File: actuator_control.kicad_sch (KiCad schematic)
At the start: 5 parts, among them J4 Conn_01x02, Q1 BSS138

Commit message: do some pcb routing
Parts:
- J7: renamed from J4; footprint Connector_JST:JST_EH_B2B-EH-A_1x02_P2.50mm_Vertical -> Connector_Molex:Molex_Micro-Fit_3.0_43650-0215_1x02_P3.00mm_Vertical
- renumbered D10 to D11, Q1 to Q2, R26 to R24, R27 to R25
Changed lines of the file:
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@@
 		(dnp no)
 		(fields_autoplaced yes)
-		(property "Reference" "D10"
+		(property "Reference" "D11"
 			(at 138.176 90.17 0)
 			(show_name no)
@@
 			(project "gse_control_node"
 				(path "/24817451-dfe0-4b9a-9d93-7304529c9d58/3ca34fcb-848a-442f-9018-9caf10b9e369"
+					(reference "D13")
+					(unit 1)
+				)
+				(path "/24817451-dfe0-4b9a-9d93-7304529c9d58/93ade7e9-ef13-409d-a430-89296b231c7f"
 					(reference "D12")
 					(unit 1)
 				)
-				(path "/24817451-dfe0-4b9a-9d93-7304529c9d58/93ade7e9-ef13-409d-a430-89296b231c7f"
+				(path "/24817451-dfe0-4b9a-9d93-7304529c9d58/c4e569fb-235e-4777-b718-8e9c9d97ed61"
+					(reference "D14")
+					(unit 1)
+				)
+				(path "/24817451-dfe0-4b9a-9d93-7304529c9d58/fe2b7ba1-9565-4f89-9bf9-1d97bef2da17"
 					(reference "D11")
-					(unit 1)
-				)
-				(path "/24817451-dfe0-4b9a-9d93-7304529c9d58/c4e569fb-235e-4777-b718-8e9c9d97ed61"
-					(reference "D13")
-					(unit 1)
-				)
-				(path "/24817451-dfe0-4b9a-9d93-7304529c9d58/fe2b7ba1-9565-4f89-9bf9-1d97bef2da17"
-					(reference "D10")
 					(unit 1)
 				)
@@
 		(dnp no)
 		(fields_autoplaced yes)
-		(property "Reference" "R27"
+		(property "Reference" "R25"
 			(at 133.35 106.6799 0)
 			(show_name no)
@@
 			(project "gse_control_node"
 				(path "/24817451-dfe0-4b9a-9d93-7304529c9d58/3ca34fcb-848a-442f-9018-9caf10b9e369"
+					(reference "R29")
+					(unit 1)
+				)
+				(path "/24817451-dfe0-4b9a-9d93-7304529c9d58/93ade7e9-ef13-409d-a430-89296b231c7f"
+					(reference "R27")
+					(unit 1)
+				)
+				(path "/24817451-dfe0-4b9a-9d93-7304529c9d58/c4e569fb-235e-4777-b718-8e9c9d97ed61"
 					(reference "R31")
 					(unit 1)
 				)
-				(path "/24817451-dfe0-4b9a-9d93-7304529c9d58/93ade7e9-ef13-409d-a430-89296b231c7f"
-					(reference "R29")
-					(unit 1)
-				)
-				(path "/24817451-dfe0-4b9a-9d93-7304529c9d58/c4e569fb-235e-4777-b718-8e9c9d97ed61"
-					(reference "R33")
-					(unit 1)
-				)
 				(path "/24817451-dfe0-4b9a-9d93-7304529c9d58/fe2b7ba1-9565-4f89-9bf9-1d97bef2da17"
-					(reference "R27")
+					(reference "R25")
 					(unit 1)
 				)
@@
 		(dnp no)
 		(fields_autoplaced yes)
-		(property "Reference" "#PWR0195"
+		(property "Reference" "#PWR071"
 			(at 130.81 97.79 0)
 			(hide yes)
@@
 			(project "gse_control_node"
 				(path "/24817451-dfe0-4b9a-9d93-7304529c9d58/3ca34fcb-848a-442f-9018-9caf10b9e369"
-					(reference "#PWR0203")
+					(reference "#PWR079")
 					(unit 1)
 				)
 				(path "/24817451-dfe0-4b9a-9d93-7304529c9d58/93ade7e9-ef13-409d-a430-89296b231c7f"
-					(reference "#PWR0197")
+					(reference "#PWR075")
 					(unit 1)
 				)
 				(path "/24817451-dfe0-4b9a-9d93-7304529c9d58/c4e569fb-235e-4777-b718-8e9c9d97ed61"
-					(reference "#PWR0207")
+					(reference "#PWR083")
 					(unit 1)
 				)
 				(path "/24817451-dfe0-4b9a-9d93-7304529c9d58/fe2b7ba1-9565-4f89-9bf9-1d97bef2da17"
-					(reference "#PWR0195")
+					(reference "#PWR071")
 					(unit 1)
 				)
@@
 		(in_pos_files yes)
 		(dnp no)
-		(property "Reference" "#PWR0198"
+		(property "Reference" "#PWR072"
 			(at 130.81 116.84 0)
 			(hide yes)
@@
 			(project "gse_control_node"
 				(path "/24817451-dfe0-4b9a-9d93-7304529c9d58/3ca34fcb-848a-442f-9018-9caf10b9e369"
-					(reference "#PWR0204")
+					(reference "#PWR080")
 					(unit 1)
 				)
 				(path "/24817451-dfe0-4b9a-9d93-7304529c9d58/93ade7e9-ef13-409d-a430-89296b231c7f"
-					(reference "#PWR0200")
+					(reference "#PWR076")
 					(unit 1)
 				)
 				(path "/24817451-dfe0-4b9a-9d93-7304529c9d58/c4e569fb-235e-4777-b718-8e9c9d97ed61"
-					(reference "#PWR0208")
+					(reference "#PWR084")
 					(unit 1)
 				)
 				(path "/24817451-dfe0-4b9a-9d93-7304529c9d58/fe2b7ba1-9565-4f89-9bf9-1d97bef2da17"
-					(reference "#PWR0198")
+					(reference "#PWR072")
 					(unit 1)
 				)
@@
 		(dnp no)
 		(fields_autoplaced yes)
-		(property "Reference" "#PWR0196"
+		(property "Reference" "#PWR073"
 			(at 146.05 96.52 0)
 			(hide yes)
@@
 			(project "gse_control_node"
 				(path "/24817451-dfe0-4b9a-9d93-7304529c9d58/3ca34fcb-848a-442f-9018-9caf10b9e369"
-					(reference "#PWR0205")
+					(reference "#PWR081")
 					(unit 1)
 				)
 				(path "/24817451-dfe0-4b9a-9d93-7304529c9d58/93ade7e9-ef13-409d-a430-89296b231c7f"
-					(reference "#PWR0201")
+					(reference "#PWR077")
 					(unit 1)
 				)
 				(path "/24817451-dfe0-4b9a-9d93-7304529c9d58/c4e569fb-235e-4777-b718-8e9c9d97ed61"
-					(reference "#PWR0209")
+					(reference "#PWR085")
 					(unit 1)
 				)
 				(path "/24817451-dfe0-4b9a-9d93-7304529c9d58/fe2b7ba1-9565-4f89-9bf9-1d97bef2da17"
-					(reference "#PWR0196")
+					(reference "#PWR073")
 					(unit 1)
 				)
@@
 		(dnp no)
 		(fields_autoplaced yes)
-		(property "Reference" "Q1"
+		(property "Reference" "Q2"
 			(at 149.86 101.5999 0)
 			(show_name no)
@@
 			(project "gse_control_node"
 				(path "/24817451-dfe0-4b9a-9d93-7304529c9d58/3ca34fcb-848a-442f-9018-9caf10b9e369"
+					(reference "Q4")
+					(unit 1)
+				)
+				(path "/24817451-dfe0-4b9a-9d93-7304529c9d58/93ade7e9-ef13-409d-a430-89296b231c7f"
 					(reference "Q3")
 					(unit 1)
 				)
-				(path "/24817451-dfe0-4b9a-9d93-7304529c9d58/93ade7e9-ef13-409d-a430-89296b231c7f"
+				(path "/24817451-dfe0-4b9a-9d93-7304529c9d58/c4e569fb-235e-4777-b718-8e9c9d97ed61"
+					(reference "Q5")
+					(unit 1)
+				)
+				(path "/24817451-dfe0-4b9a-9d93-7304529c9d58/fe2b7ba1-9565-4f89-9bf9-1d97bef2da17"
 					(reference "Q2")
-					(unit 1)
-				)
-				(path "/24817451-dfe0-4b9a-9d93-7304529c9d58/c4e569fb-235e-4777-b718-8e9c9d97ed61"
-					(reference "Q4")
-					(unit 1)
-				)
-				(path "/24817451-dfe0-4b9a-9d93-7304529c9d58/fe2b7ba1-9565-4f89-9bf9-1d97bef2da17"
-					(reference "Q1")
 					(unit 1)
 				)
@@
 		(dnp no)
 		(fields_autoplaced yes)
-		(property "Reference" "J4"
+		(property "Reference" "J7"
 			(at 153.67 93.9799 0)
 			(show_name no)
@@
 			)
 		)
-		(property "Footprint" "Connector_JST:JST_EH_B2B-EH-A_1x02_P2.50mm_Vertical"
+		(property "Footprint" "Connector_Molex:Molex_Micro-Fit_3.0_43650-0215_1x02_P3.00mm_Vertical"
 			(at 151.13 93.98 0)
 			(hide yes)
@@
 			(project "gse_control_node"
 				(path "/24817451-dfe0-4b9a-9d93-7304529c9d58/3ca34fcb-848a-442f-9018-9caf10b9e369"
-					(reference "J6")
+					(reference "J9")
 					(unit 1)
 				)
 				(path "/24817451-dfe0-4b9a-9d93-7304529c9d58/93ade7e9-ef13-409d-a430-89296b231c7f"
-					(reference "J5")
+					(reference "J8")
 					(unit 1)
 				)
 				(path "/24817451-dfe0-4b9a-9d93-7304529c9d58/c4e569fb-235e-4777-b718-8e9c9d97ed61"
-					(reference "J9")
+					(reference "J10")
 					(unit 1)
 				)
 				(path "/24817451-dfe0-4b9a-9d93-7304529c9d58/fe2b7ba1-9565-4f89-9bf9-1d97bef2da17"
-					(reference "J4")
+					(reference "J7")
 					(unit 1)
 				)
@@
 		(dnp no)
 		(fields_autoplaced yes)
-		(property "Reference" "R26"
+		(property "Reference" "R24"
 			(at 124.46 99.06 90)
 			(show_name no)
@@
 			(project "gse_control_node"
 				(path "/24817451-dfe0-4b9a-9d93-7304529c9d58/3ca34fcb-848a-442f-9018-9caf10b9e369"
+					(reference "R28")
+					(unit 1)
+				)
+				(path "/24817451-dfe0-4b9a-9d93-7304529c9d58/93ade7e9-ef13-409d-a430-89296b231c7f"
+					(reference "R26")
+					(unit 1)
+				)
+				(path "/24817451-dfe0-4b9a-9d93-7304529c9d58/c4e569fb-235e-4777-b718-8e9c9d97ed61"
 					(reference "R30")
 					(unit 1)
 				)
-				(path "/24817451-dfe0-4b9a-9d93-7304529c9d58/93ade7e9-ef13-409d-a430-89296b231c7f"
-					(reference "R28")
-					(unit 1)
-				)
-				(path "/24817451-dfe0-4b9a-9d93-7304529c9d58/c4e569fb-235e-4777-b718-8e9c9d97ed61"
-					(reference "R32")
-					(unit 1)
-				)
 				(path "/24817451-dfe0-4b9a-9d93-7304529c9d58/fe2b7ba1-9565-4f89-9bf9-1d97bef2da17"
-					(reference "R26")
+					(reference "R24")
 					(unit 1)
 				)
@@
 		(in_pos_files yes)
 		(dnp no)
-		(property "Reference" "#PWR0199"
+		(property "Reference" "#PWR074"
 			(at 146.05 116.84 0)
 			(hide yes)
@@
 			(project "gse_control_node"
 				(path "/24817451-dfe0-4b9a-9d93-7304529c9d58/3ca34fcb-848a-442f-9018-9caf10b9e369"
-					(reference "#PWR0206")
+					(reference "#PWR082")
 					(unit 1)
 				)
 				(path "/24817451-dfe0-4b9a-9d93-7304529c9d58/93ade7e9-ef13-409d-a430-89296b231c7f"
-					(reference "#PWR0202")
+					(reference "#PWR078")
 					(unit 1)
 				)
 				(path "/24817451-dfe0-4b9a-9d93-7304529c9d58/c4e569fb-235e-4777-b718-8e9c9d97ed61"
-					(reference "#PWR0210")
+					(reference "#PWR086")
 					(unit 1)
 				)
 				(path "/24817451-dfe0-4b9a-9d93-7304529c9d58/fe2b7ba1-9565-4f89-9bf9-1d97bef2da17"
-					(reference "#PWR0199")
-					(unit 1)
-				)
+					(reference "#PWR074")
+					(unit 1)
+				)

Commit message: remove unneccesary component fields
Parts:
- D11: MPN SK44BL-TP -> (none)
- J7: LCSC (none) -> N/A; now left out of the parts list
- Q2: DK_Datasheet_Link https://www.onsemi.com/pub/Collateral/BSS138-D.PDF -> (none); DK_Detail_Page /product-detail/en/on-semiconductor/BSS138/BSS138CT-ND/2442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 -> (none); Description_1 MOSFET N-CH 50V 220MA SOT-23 -> (none); Family Transistors - FETs, MOSFETs - Single -> (none); LCSC C8490 -> C82045; MPN BSS138 -> (none); Manufacturer ON Semiconductor -> (none); Status Active -> (none)
- R24: value 100 -> 100Ω; LCSC C25076 -> (none); MPN 0402WGF1000TCE -> (none)
- R25: value 100k -> 100kΩ; LCSC C25530 -> (none); MPN 0402WGJ0104TCE -> (none)
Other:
- moved on the sheet: D11, J7, Q2, R24, R25

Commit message: add all lcsc part numbers
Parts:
- R24: LCSC (none) -> C106232
- R25: LCSC (none) -> C122538
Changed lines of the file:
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@@
 			)
 		)
-		(property "LCSC" ""
+		(property "LCSC" "C122538"
 			(at 95.25 69.85 0)
 			(hide yes)
@@
 			)
 		)
-		(property "LCSC" ""
+		(property "LCSC" "C106232"
 			(at 88.9 67.31 90)
 			(hide yes)

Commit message: add a 12v testpoint
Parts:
- R24: LCSC C106232 -> (none)
- R25: LCSC C122538 -> (none)
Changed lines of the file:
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@@
 			)
 		)
-		(property "LCSC" "C122538"
+		(property "LCSC" ""
 			(at 95.25 69.85 0)
 			(hide yes)
@@
 			)
 		)
-		(property "LCSC" "C106232"
+		(property "LCSC" ""
 			(at 88.9 67.31 90)
 			(hide yes)

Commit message: update resistors to jlcpcb basic components
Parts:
- R24: footprint Resistor_SMD:R_0402_1005Metric -> Resistor_SMD:R_0603_1608Metric
- R25: LCSC (none) -> C122538
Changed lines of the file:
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@@
 			)
 		)
-		(property "LCSC" ""
+		(property "LCSC" "C122538"
 			(at 95.25 69.85 0)
 			(hide yes)
@@
 			)
 		)
-		(property "Footprint" "Resistor_SMD:R_0402_1005Metric"
+		(property "Footprint" "Resistor_SMD:R_0603_1608Metric"
 			(at 88.9 67.31 0)
 			(hide yes)

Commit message: remove some extended components from bom (to be handsoldered)
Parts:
- D11, Q2: now left out of the parts list
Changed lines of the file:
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@@
 		(body_style 1)
 		(exclude_from_sim no)
-		(in_bom yes)
-		(on_board yes)
-		(in_pos_files yes)
+		(in_bom no)
+		(on_board yes)
+		(in_pos_files no)
 		(dnp no)
 		(fields_autoplaced yes)
@@
 		(body_style 1)
 		(exclude_from_sim no)
-		(in_bom yes)
-		(on_board yes)
-		(in_pos_files yes)
+		(in_bom no)
+		(on_board yes)
+		(in_pos_files no)
 		(dnp no)
 		(fields_autoplaced yes)

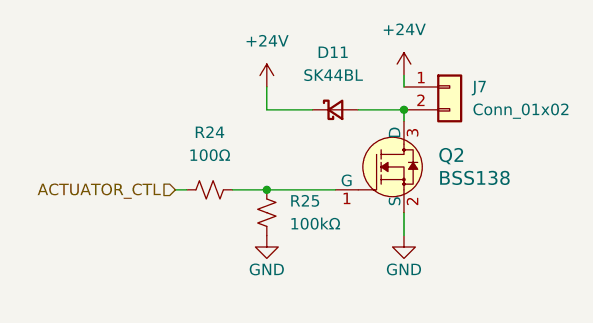
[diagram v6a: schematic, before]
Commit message: add tachometer pullup and pwm low side fet for fans
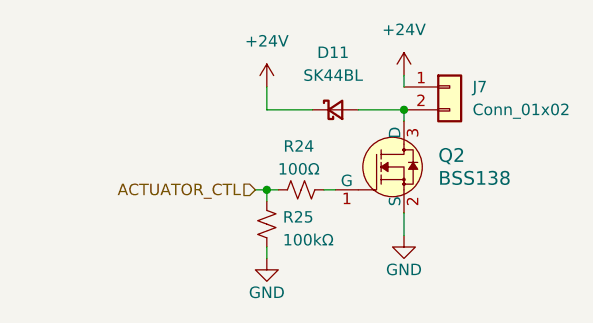
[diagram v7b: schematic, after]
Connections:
- net ACTUATOR_CTL: now also R25.1
- net at Q2.1 (G), R24.2: no longer R25.1
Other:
- moved on the sheet: R24, R25
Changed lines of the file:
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@@
+	(wire
+		(pts
+			(xy 96.52 67.31) (xy 95.25 67.31)
+		)
+		(stroke
+			(width 0)
+			(type default)
+		)
+	)
 	(wire
 		(pts
@@
 	(wire
 		(pts
+			(xy 93.98 67.31) (xy 95.25 67.31)
+		)
+		(stroke
+			(width 0)
+			(type default)
+		)
+	)
+	(wire
+		(pts
+			(xy 95.25 74.93) (xy 95.25 73.66)
+		)
+		(stroke
+			(width 0)
+			(type default)
+		)
+	)
+	(wire
+		(pts
 			(xy 110.49 69.85) (xy 110.49 72.39)
 		)
@@
 	(wire
 		(pts
-			(xy 95.25 67.31) (xy 102.87 67.31)
+			(xy 95.25 67.31) (xy 95.25 68.58)
 		)
 		(stroke
@@
 	(wire
 		(pts
-			(xy 85.09 67.31) (xy 86.36 67.31)
-		)
-		(stroke
-			(width 0)
-			(type default)
-		)
-	)
-	(wire
-		(pts
-			(xy 91.44 67.31) (xy 95.25 67.31)
+			(xy 101.6 67.31) (xy 102.87 67.31)
 		)
 		(stroke
@@
 	(hierarchical_label "ACTUATOR_CTL"
 		(shape input)
-		(at 85.09 67.31 180)
+		(at 93.98 67.31 180)
 		(effects
 			(font
@@
 	(symbol
 		(lib_id "Device:R_Small_US")
-		(at 95.25 69.85 0)
+		(at 95.25 71.12 0)
 		(unit 1)
 		(body_style 1)
@@
 		(in_pos_files yes)
 		(dnp no)
-		(fields_autoplaced yes)
 		(property "Reference" "R25"
-			(at 97.79 68.5799 0)
+			(at 97.028 70.358 0)
 			(show_name no)
 			(do_not_autoplace no)
@@
 		)
 		(property "Value" "100kΩ"
-			(at 97.79 71.1199 0)
+			(at 97.028 72.898 0)
 			(show_name no)
 			(do_not_autoplace no)
@@
 		)
 		(property "Footprint" "Resistor_SMD:R_0603_1608Metric"
-			(at 95.25 69.85 0)
+			(at 95.25 71.12 0)
 			(hide yes)
 			(show_name no)
@@
 		)
 		(property "Datasheet" ""
-			(at 95.25 69.85 0)
+			(at 95.25 71.12 0)
 			(hide yes)
 			(show_name no)
@@
 		)
 		(property "Description" "Resistor, small US symbol"
-			(at 95.25 69.85 0)
+			(at 95.25 71.12 0)
 			(hide yes)
 			(show_name no)
@@
 		)
 		(property "LCSC" "C122538"
-			(at 95.25 69.85 0)
+			(at 95.25 71.12 0)
 			(hide yes)
 			(show_name no)
@@
 	(symbol
 		(lib_id "power:GND")
-		(at 95.25 72.39 0)
+		(at 95.25 74.93 0)
 		(unit 1)
 		(body_style 1)
@@
 		(dnp no)
 		(property "Reference" "#PWR072"
+			(at 95.25 81.28 0)
+			(hide yes)
+			(show_name no)
+			(do_not_autoplace no)
+			(effects
+				(font
+					(size 1.27 1.27)
+				)
+			)
+		)
+		(property "Value" "GND"
 			(at 95.25 78.74 0)
-			(hide yes)
-			(show_name no)
-			(do_not_autoplace no)
-			(effects
-				(font
-					(size 1.27 1.27)
-				)
-			)
-		)
-		(property "Value" "GND"
-			(at 95.25 76.2 0)
 			(show_name no)
 			(do_not_autoplace no)
@@
 		)
 		(property "Footprint" ""
-			(at 95.25 72.39 0)
+			(at 95.25 74.93 0)
 			(hide yes)
 			(show_name no)
@@
 		)
 		(property "Datasheet" ""
-			(at 95.25 72.39 0)
+			(at 95.25 74.93 0)
 			(hide yes)
 			(show_name no)
@@
 		)
 		(property "Description" "Power symbol creates a global label with name \"GND\" , ground"
-			(at 95.25 72.39 0)
+			(at 95.25 74.93 0)
 			(hide yes)
 			(show_name no)
@@
 	(symbol
 		(lib_id "Device:R_Small_US")
-		(at 88.9 67.31 90)
+		(at 99.06 67.31 90)
 		(unit 1)
 		(body_style 1)
@@
 		(in_pos_files yes)
 		(dnp no)
-		(fields_autoplaced yes)
 		(property "Reference" "R24"
-			(at 88.9 60.96 90)
+			(at 98.806 62.484 90)
 			(show_name no)
 			(do_not_autoplace no)
@@
 		)
 		(property "Value" "100Ω"
-			(at 88.9 63.5 90)
+			(at 98.806 65.024 90)
 			(show_name no)
 			(do_not_autoplace no)
@@
 		)
 		(property "Footprint" "Resistor_SMD:R_0603_1608Metric"
-			(at 88.9 67.31 0)
+			(at 99.06 67.31 0)
 			(hide yes)
 			(show_name no)
@@
 		)
 		(property "Datasheet" ""
-			(at 88.9 67.31 0)
+			(at 99.06 67.31 0)
 			(hide yes)
 			(show_name no)
@@
 		)
 		(property "Description" "Resistor, small US symbol"
-			(at 88.9 67.31 0)
+			(at 99.06 67.31 0)
 			(hide yes)
 			(show_name no)
@@
 		)
 		(property "LCSC" ""
-			(at 88.9 67.31 90)
-			(hide yes)
-			(show_name no)
+			(at 99.06 67.31 90)
+			(hide yes)
+			(show_name no)

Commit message: add back bss138 to jlcpcb bom
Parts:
- Q2: now in the parts list
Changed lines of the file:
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@@
 		(body_style 1)
 		(exclude_from_sim no)
-		(in_bom no)
+		(in_bom yes)
 		(on_board yes)
-		(in_pos_files no)
+		(in_pos_files yes)
 		(dnp no)
 		(fields_autoplaced yes)
